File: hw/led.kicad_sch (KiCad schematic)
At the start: 20 parts, among them J4 LED_OUT

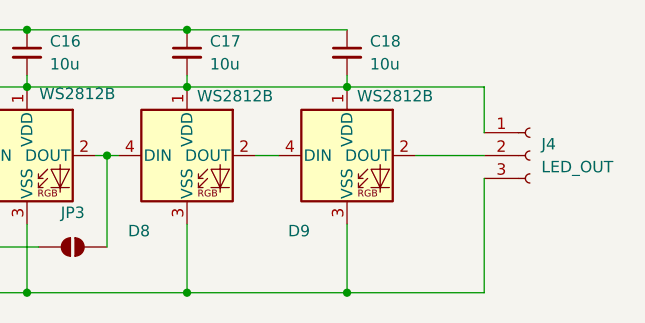
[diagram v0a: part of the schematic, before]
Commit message: USB fix and schematic cleanup (April work)
Add CR2 ESDA25P35 on the USB lines and tie VBUS straight to +5V, drop
the ESP_PWR header J7, JP9 and the VBAT_MON divider, add R25 4.7k and
wire the LSM303C I2C, remove the external LED output (D9, J4, C18).
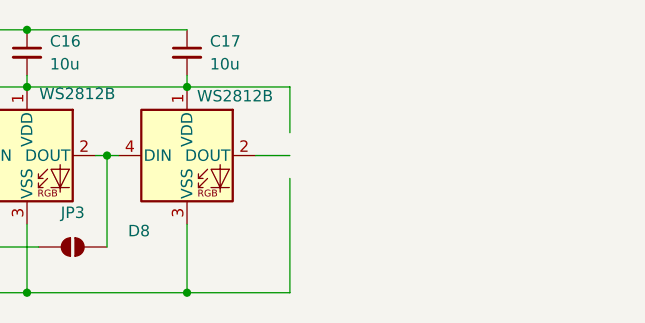
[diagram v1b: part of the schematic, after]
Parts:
- removed C18: 10u, Capacitor_SMD:C_0603_1608Metric, symbol Device:C_Small
- removed D9: WS2812B, LED_SMD:LED_WS2812B_PLCC4_5.0x5.0mm_P3.2mm, symbol LED:WS2812B
- removed J4: LED_OUT, Connector_JST:JST_EH_B3B-EH-A_1x03_P2.50mm_Vertical, symbol Connector:Conn_01x03_Socket
